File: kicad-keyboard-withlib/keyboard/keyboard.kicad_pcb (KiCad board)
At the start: 2 copper layers, 45 parts, among them SW1 SW_Push, SW10 SW_Push, SW11 SW_Push, SW12 SW_Push, SW13 SW_Push, SW14 SW_Push, SW15 SW_Push, SW16 SW_Push, SW17 SW_Push, SW18 SW_Push, SW19 SW_Push, SW2 SW_Push, SW20 SW_Push, SW21 SW_Push, SW22 SW_Push, SW23 SW_Push, SW24 SW_Push, SW25 SW_Push, SW26 SW_Push, SW27 SW_Push, SW28 SW_Push, SW29 SW_Push, SW3 SW_Push, SW30 SW_Push, SW31 SW_Push, SW32 SW_Push, SW33 SW_Push, SW34 SW_Push, SW35 SW_Push, SW36 SW_Push, SW37 SW_Push, SW38 SW_Push, SW4 SW_Push, SW41 RotaryEncoder_Switch, SW42 SW_Wuerth_450301014042, SW5 SW_Push, SW6 SW_Push, SW7 SW_Push, SW8 SW_Push, SW9 SW_Push, U2 MCP23017_SO

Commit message: mid pcb commit in case of a kernel panic
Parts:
- moved SW42 74.9 mm to (149.0, 59.5), turned to 0 degrees
- moved P1 8.50 mm to (28.2, 42.5)
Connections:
- P1 pad 17: Net-(SW42-B) -> Net-(SW42-C)
- P1 pad 18: Net-(SW42-A) -> Net-(SW42-B)
- P1 pad 19: Net-(SW42-C) -> Net-(SW42-A)
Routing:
- net Net-(P1-R4): track 0.00 -> 319.4 mm
- net Net-(P1-R3): track 0.00 -> 292.4 mm
- net Net-(P1-R2): track 0.00 -> 267.9 mm
- net Net-(P1-R1): track 0.00 -> 246.0 mm
- net Net-(P1-C10): track 0.00 -> 143.1 mm
- net Net-(P1-C9): track 0.00 -> 128.1 mm
- net Net-(P1-C2): track 0.00 -> 127.2 mm, vias 0 -> 8
- net Net-(P1-C1): track 0.00 -> 126.4 mm, vias 0 -> 8
- net Net-(P1-C8): track 0.00 -> 113.2 mm
- net Net-(P1-C7): track 0.00 -> 98.2 mm
- net Net-(P1-C6): track 0.00 -> 83.3 mm
- net Net-(SW42-B): track 0.00 -> 78.6 mm
- net Net-(SW42-C): track 0.00 -> 78.6 mm
- net Net-(SW42-A): track 0.00 -> 78.6 mm
- net Net-(P1-C5): track 0.00 -> 68.3 mm
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
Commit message: check point pcb keyboard
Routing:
- net Net-(P1-R1): track 246.0 -> 371.0 mm
- net Net-(P1-R3): track 292.4 -> 417.4 mm
- net Net-(P1-R2): track 267.9 -> 392.9 mm
- net Net-(P1-C8): track 113.2 -> 235.9 mm, vias 0 -> 6
- net Net-(P1-R4): track 319.4 -> 420.2 mm
- net Net-(P1-C6): track 83.3 -> 171.6 mm, vias 0 -> 8
- net Net-(P1-C4): track 53.3 -> 141.4 mm, vias 0 -> 8
- net Net-(P1-C3): track 44.5 -> 132.5 mm, vias 0 -> 8
- net Net-(P1-C7): track 98.2 -> 186.2 mm, vias 0 -> 8
- net Net-(P1-C5): track 68.3 -> 156.3 mm, vias 0 -> 8
- net Net-(P1-C10): track 143.1 -> 200.5 mm
- net Net-(P1-C9): track 128.1 -> 182.6 mm, vias 0 -> 6

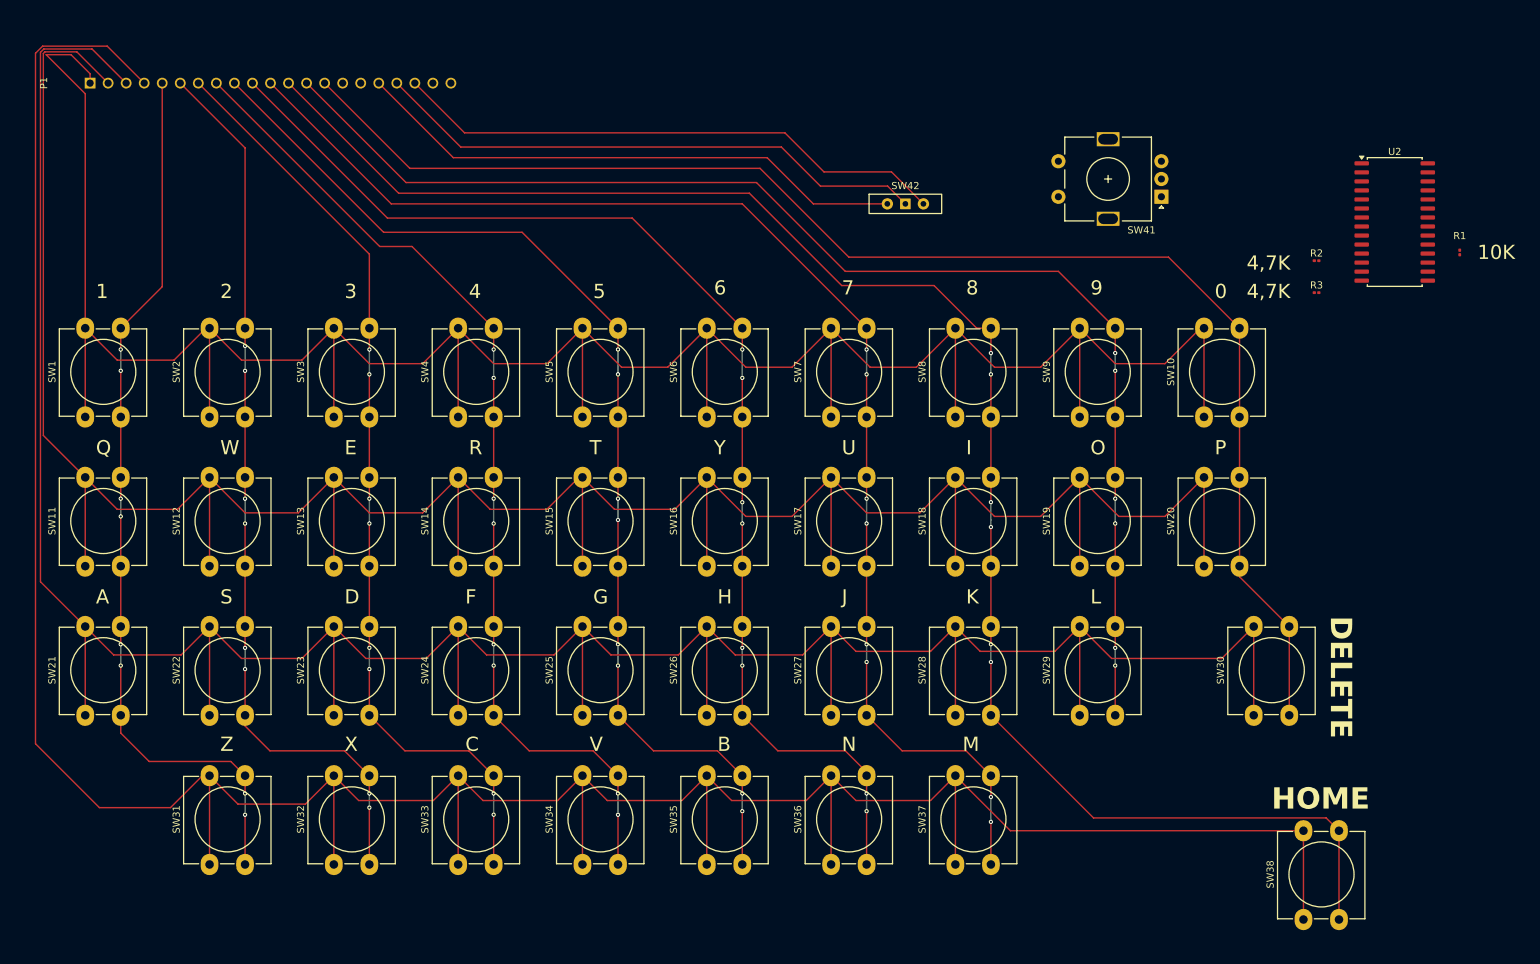
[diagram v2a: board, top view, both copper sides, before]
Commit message: to change: i2c to tht, else everything else is linked
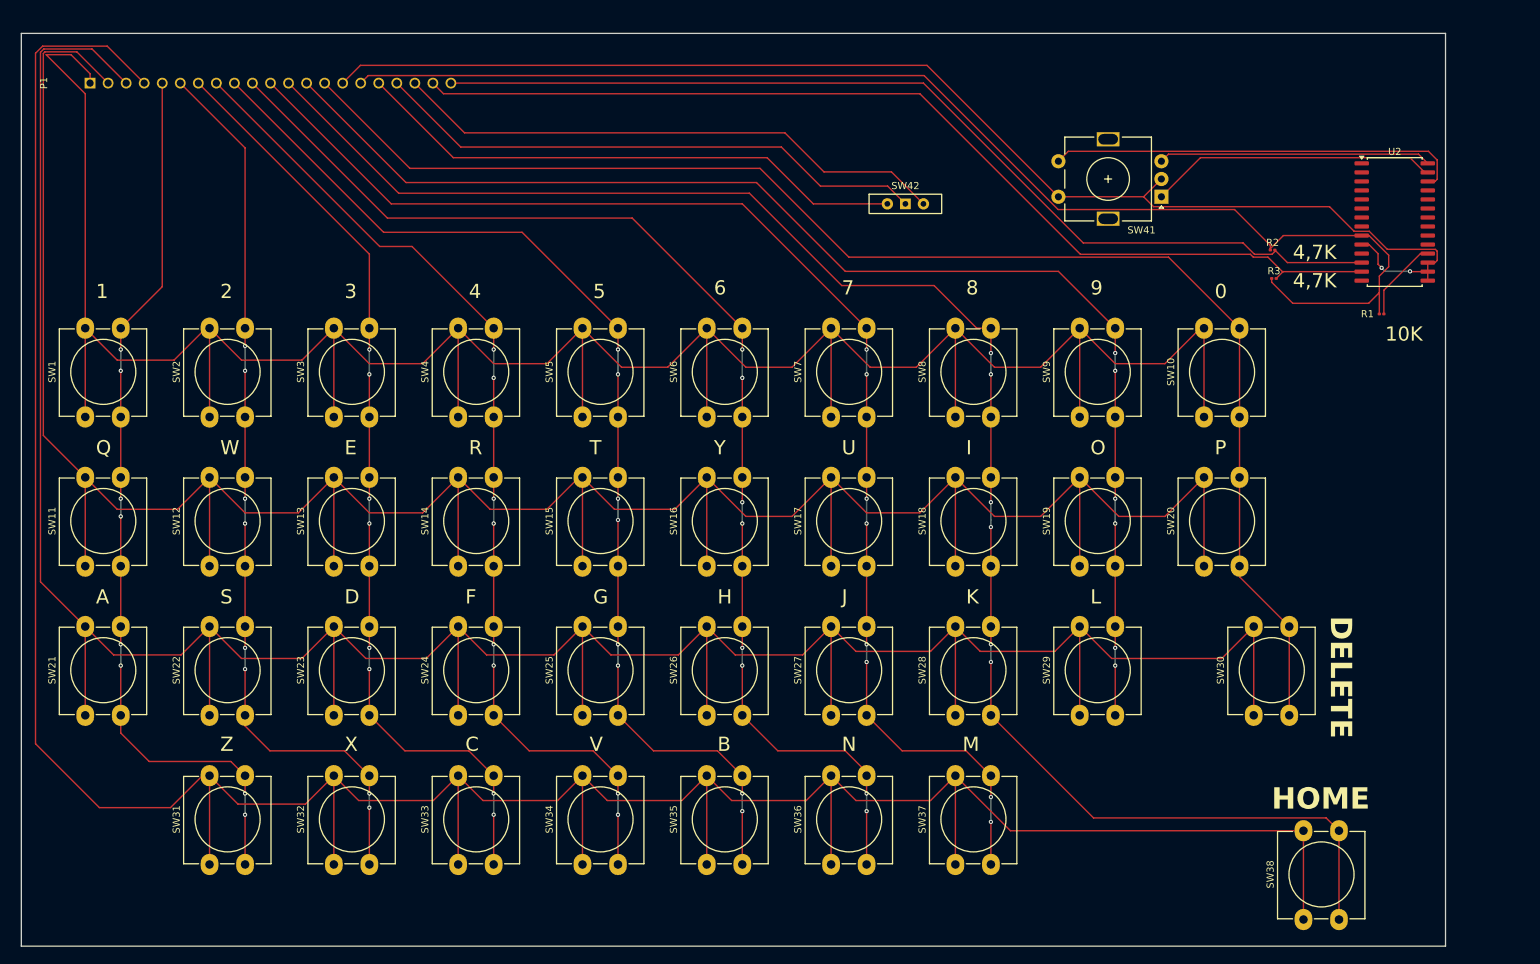
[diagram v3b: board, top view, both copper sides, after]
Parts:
- moved R1 14.0 mm to (216.0, 75.0), turned to 0 degrees
- moved R2 6.37 mm to (200.7, 66.0)
- moved R3 6.32 mm to (200.8, 70.0)
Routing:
- net Net-(P1-GND): track 0.00 -> 186.5 mm, vias 0 -> 2
- net Net-(P1-VCC): track 0.00 -> 184.2 mm
- net Net-(P1-SDA): track 0.00 -> 143.1 mm
- net Net-(P1-SCL): track 0.00 -> 139.3 mm
- net Net-(U2-GPA5): track 0.00 -> 58.6 mm
- net Net-(U2-GPA6): track 0.00 -> 40.6 mm
- net Net-(U2-GPA7): track 0.00 -> 38.5 mm
- net Net-(U2-~{RESET}): track 0.00 -> 11.7 mm
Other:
- board outline added: 200.5 x 128.5 mm

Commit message: add: better slide switch, have to edit vcc
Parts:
- removed SW42: SW_Wuerth_450301014042, Button_Switch_THT:SW_Slide-03_Wuerth-WS-SLTV_10x2.5x6.4_P2.54mm
- added SW39: SW_Slide_DPDT, Button_Switch_THT:SW_CK_JS202011CQN_DPDT_Straight, F.Cu at (144.5, 56.2)
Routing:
- net Net-(P1-SLD_SW-Pad19): track 78.6 -> 75.3 mm
- net Net-(P1-SLD_SW-Pad18): track 78.6 -> 75.3 mm
- net Net-(P1-SLD_SW-Pad17): track 78.6 -> 75.4 mm

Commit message: quick fix
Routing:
- net Net-(P1-VCC): track 184.2 -> 183.5 mm

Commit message: fix post Christian
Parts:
- R1, R2, R3: value Heater -> R; footprint Resistor_SMD:R_0201_0603Metric -> Resistor_SMD:R_0603_1608Metric_Pad0.98x0.95mm_HandSolder
- moved R3 5.07 mm to (200.0, 65.0), turned to 90 degrees
- moved R2 5.01 mm to (201.0, 71.0), turned to 90 degrees
- moved R1 1.41 mm to (217.0, 76.0)
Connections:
- net Net-(P1-GND) renamed /GND
- R2 pad 2: Net-(P1-SCL) -> Net-(P1-SDA)
- R3 pad 1: Net-(P1-VCC) -> Net-(P1-SCL)
- R3 pad 2: Net-(P1-SDA) -> Net-(P1-VCC)
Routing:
- net /GND: track 186.5 -> 9.77 mm, vias 2 -> 4
- net Net-(P1-R1): track 371.0 -> 355.4 mm
- net Net-(P1-R4): track 420.2 -> 410.5 mm
- net Net-(P1-R2): track 392.9 -> 386.5 mm
- net Net-(P1-R3): track 417.4 -> 412.2 mm
- net Net-(U2-GPA5): track 58.6 -> 59.9 mm
- net Net-(P1-SCL): track 139.3 -> 138.7 mm
- added copper zone on B.Cu, net /GND
